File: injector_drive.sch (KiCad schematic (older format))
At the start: 10 parts, among them P54 CONN_1, P55 CONN_1, Q17 2N6044, U15 LM1949

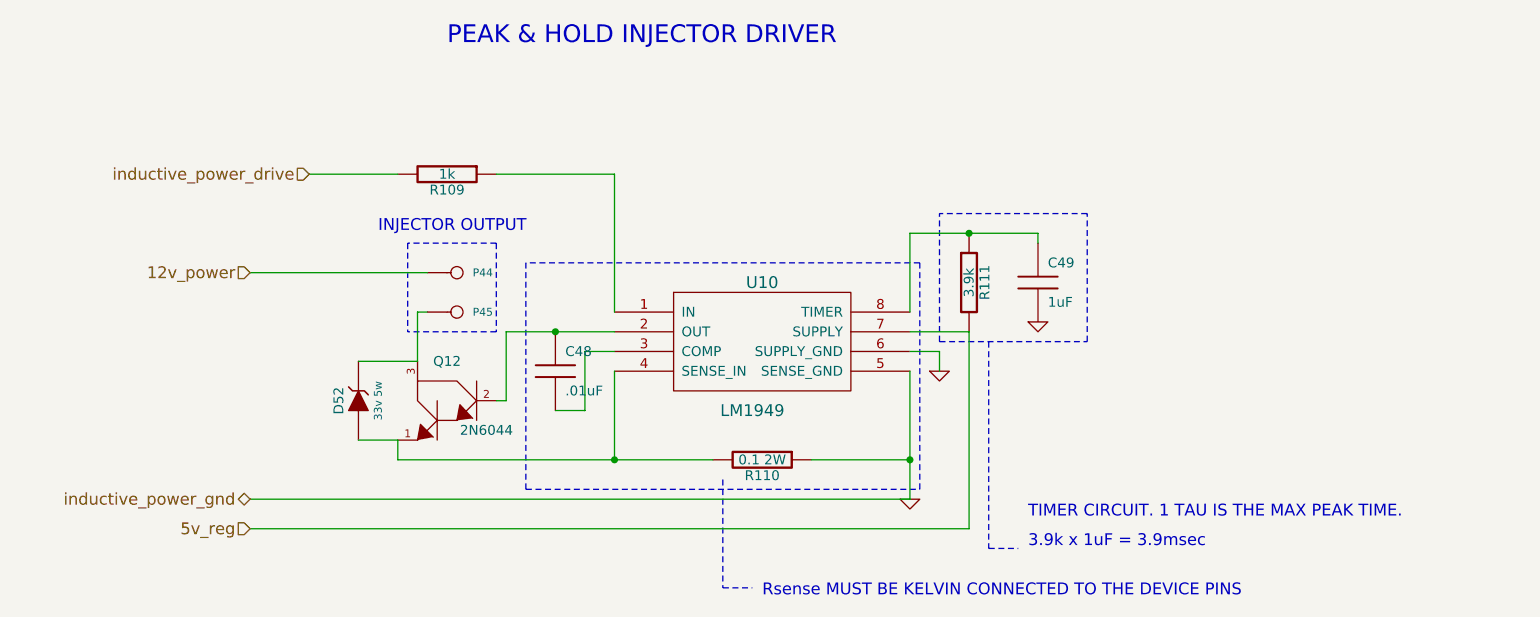
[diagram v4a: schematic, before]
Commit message: MAP circuit compatible with external sensors. Baro is left untouched
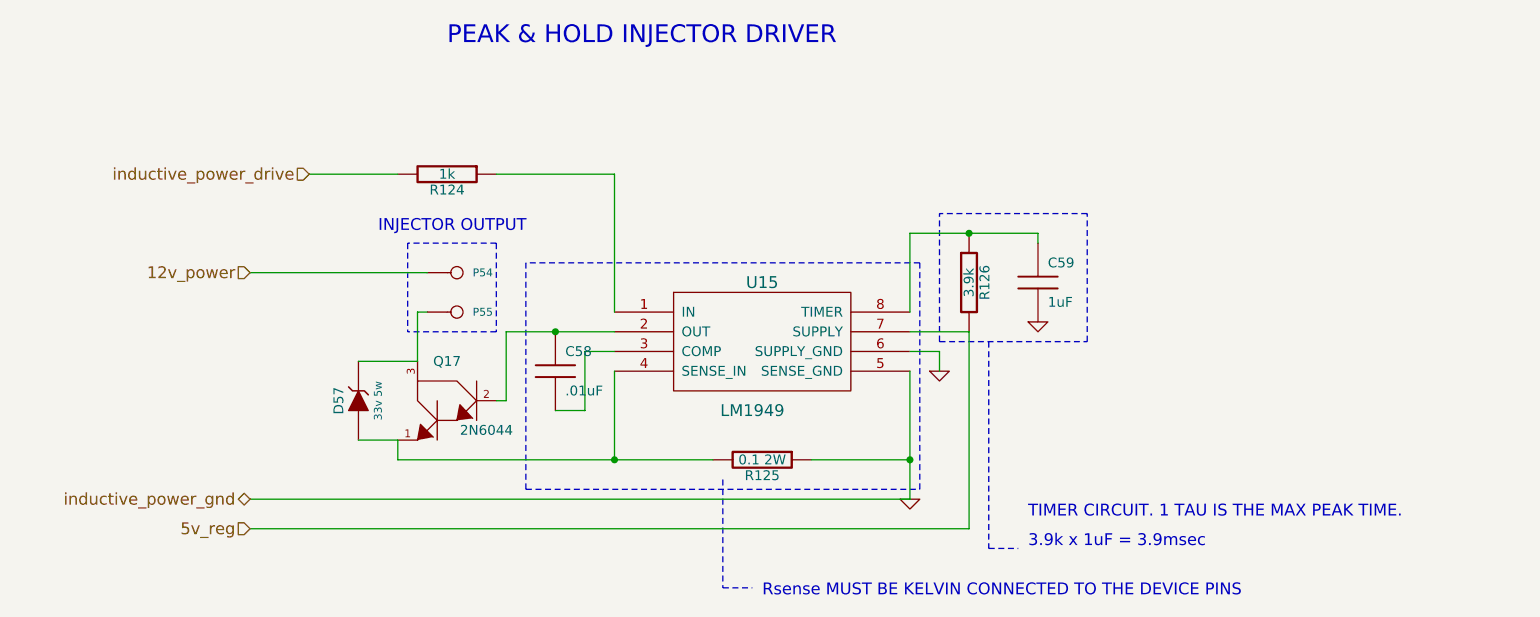
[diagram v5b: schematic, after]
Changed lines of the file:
@@
-EESchema Schematic File Version 2  date Thu 22 Jul 2010 10:06:33 AM ART
+EESchema Schematic File Version 2  date Sat 24 Jul 2010 11:01:40 AM ART
 LIBS:power
 LIBS:freeEMS_lib
@@
 Sheet 7 41
 Title "freeEMS 1.0"
-Date "22 jul 2010"
+Date "24 jul 2010"
 Rev "A.07"
 Comp "diyefi.org"
@@
 AR Path="/4C2F3DD9/4C2ED144" Ref="C51"  Part="1"
 AR Path="/4C2F3BE4/4C2ED144" Ref="C49"  Part="1"
-F 0 "C49" H 6650 2650 50  0000 L CNN
+F 0 "C59" H 6650 2650 50  0000 L CNN
 F 1 "1uF" H 6650 2450 50  0000 L CNN
 	1    6600 2550
@@
 AR Path="/4C2F3DD9/4C2ED135" Ref="R114"  Part="1"
 AR Path="/4C2F3BE4/4C2ED135" Ref="R111"  Part="1"
-F 0 "R111" V 6330 2550 50  0000 C CNN
+F 0 "R126" V 6330 2550 50  0000 C CNN
 F 1 "3.9k" V 6250 2550 50  0000 C CNN
 	1    6250 2550
@@
 AR Path="/4C2F3DD9/4C2ED0C2" Ref="D53"  Part="1"
 AR Path="/4C2F3BE4/4C2ED0C2" Ref="D52"  Part="1"
-F 0 "D52" H 3150 3250 50  0000 C CNN
+F 0 "D57" H 3150 3250 50  0000 C CNN
 F 1 "33v 5w" H 3150 3050 40  0000 C CNN
 	1    3150 3150
@@
 AR Path="/4C2F3DD9/4C2ED077" Ref="R113"  Part="1"
 AR Path="/4C2F3BE4/4C2ED077" Ref="R110"  Part="1"
-F 0 "R110" V 5280 3450 50  0000 C CNN
+F 0 "R125" V 5280 3450 50  0000 C CNN
 F 1 "0.1 2W" V 5200 3450 50  0000 C CNN
 	1    5200 3450
@@
 AR Path="/4C2F3DD9/4C2ED01B" Ref="C50"  Part="1"
 AR Path="/4C2F3BE4/4C2ED01B" Ref="C48"  Part="1"
-F 0 "C48" H 4200 3100 50  0000 L CNN
+F 0 "C58" H 4200 3100 50  0000 L CNN
 F 1 ".01uF" H 4200 2900 50  0000 L CNN
 	1    4150 3000
@@
 AR Path="/4C2F3DD9/4C2ECF62" Ref="Q13"  Part="1"
 AR Path="/4C2F3BE4/4C2ECF62" Ref="Q12"  Part="1"
-F 0 "Q12" H 3600 3450 50  0000 C CNN
+F 0 "Q17" H 3600 3450 50  0000 C CNN
 F 1 "2N6044" H 3400 3100 50  0000 C CNN
 	1    3600 3200
@@
 AR Path="/4C2F3DD9/4C2ECEC5" Ref="U11"  Part="1"
 AR Path="/4C2F3BE4/4C2ECEC5" Ref="U10"  Part="1"
-F 0 "U10" H 5200 3150 60  0000 C CNN
+F 0 "U15" H 5200 3150 60  0000 C CNN
 F 1 "LM1949" H 5150 2500 60  0000 C CNN
 F 2 "8dip300" H 5260 3210 60  0001 C CNN
@@
 AR Path="/4C2F3DD9/48AA1A76" Ref="P47"  Part="1"
 AR Path="/4C2F3BE4/48AA1A76" Ref="P45"  Part="1"
-F 0 "P45" H 3730 2700 40  0000 L CNN
+F 0 "P55" H 3730 2700 40  0000 L CNN
 F 1 "CONN_1" H 3650 2755 30  0001 C CNN
 F 2 "1PIN" V -2870 3300 60  0001 C CNN
@@
 AR Path="/4C2F3DD9/48AA1A73" Ref="P46"  Part="1"
 AR Path="/4C2F3BE4/48AA1A73" Ref="P44"  Part="1"
-F 0 "P44" H 3730 2500 40  0000 L CNN
+F 0 "P54" H 3730 2500 40  0000 L CNN
 F 1 "CONN_1" H 3650 2555 30  0001 C CNN
 F 2 "1PIN" V -2870 3300 60  0001 C CNN
@@
 AR Path="/4C2F3DD9/4C2F52D2" Ref="R112"  Part="1"
 AR Path="/4C2F3BE4/4C2F52D2" Ref="R109"  Part="1"
-F 0 "R109" V 3680 2000 50  0000 C CNN
+F 0 "R124" V 3680 2000 50  0000 C CNN
 F 1 "1k" V 3600 2000 50  0000 C CNN
 F 2 "R4-SM0805" V 3780 2100 60  0001 C CNN
